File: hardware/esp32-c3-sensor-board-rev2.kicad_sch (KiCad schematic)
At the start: 14 parts, among them J1 BME280_Module, J2 BH1750_Module, J3 Relay, J4 Button, J5 GPIO, U1 ESP32-C3-SuperMini, U2 HLK-LD2410C

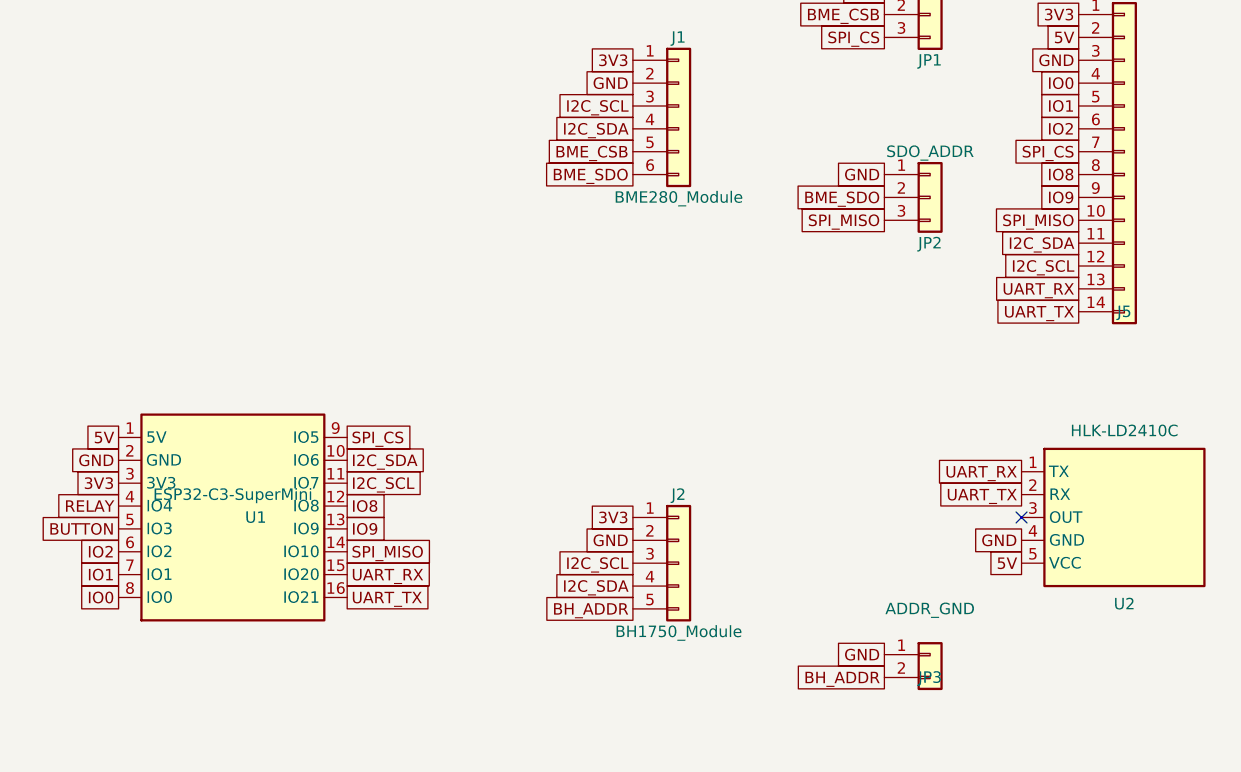
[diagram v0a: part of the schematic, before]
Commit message: Fix ESP32-C3 Super Mini pinout and re-route rev2
- Correct the U1 socket footprint pad order to match the physical module
  (pad 1 = 5V at the USB end, pad 8 = GPIO0, pad 9 = GPIO5, pad 16 = GPIO21).
- Use the reference pinout for I2C: SDA = GPIO8, SCL = GPIO9; free GPIO6/7
  go to the J5 breakout row. UART stays GPIO20/21, relay GPIO4, button GPIO3.
- Add full pin descriptions to the ESP32 symbol and board silkscreen
  (GPIOx plus MISO/MOSI/SS/SDA/SCL/RX/TX), and update all docs.
- Re-route the board against the corrected pin order (FreeRouting);
  DRC 0 errors / 0 unconnected, 2 pre-existing cosmetic silk warnings.
- Regenerate gerbers, drill, job file and the gerber zip.

doorbell.yml still lists GPIO6/7 for I2C and must be updated to
sda: GPIO8 / scl: GPIO9 on the software side.

Co-Authored-By: Claude Code <noreply@anthropic.com>
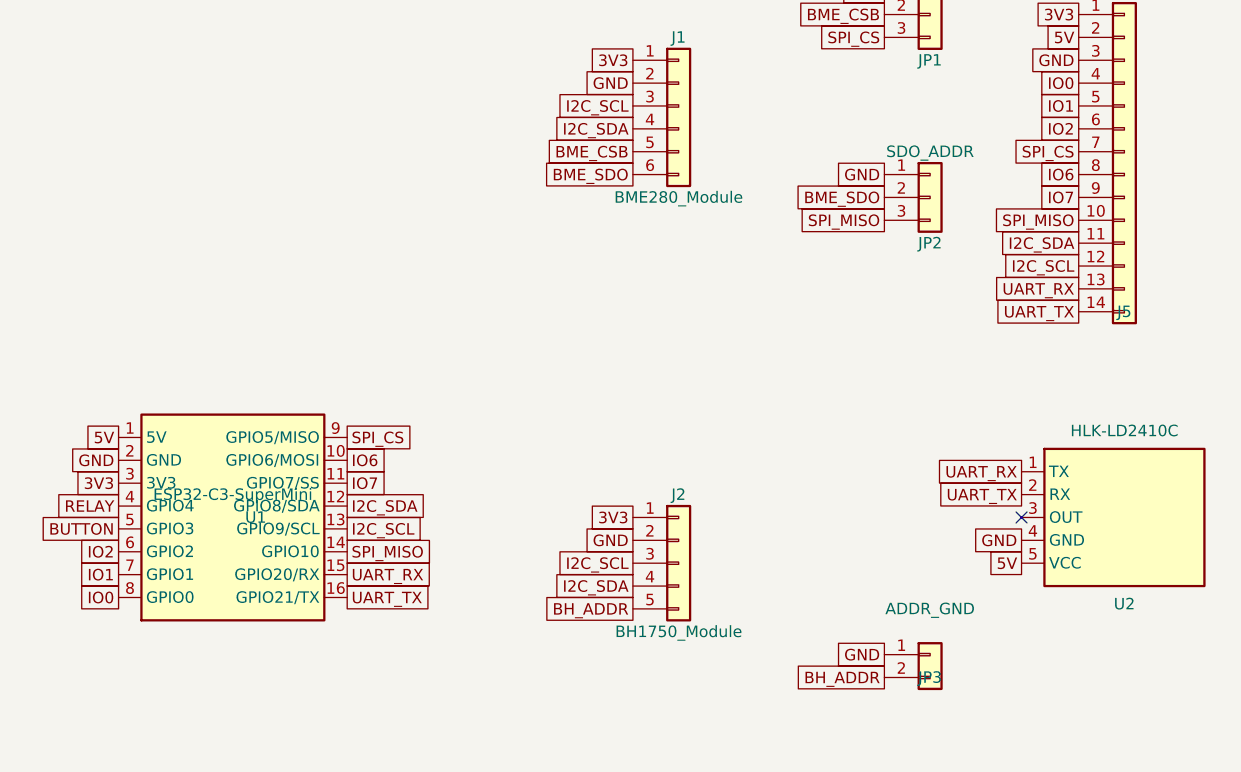
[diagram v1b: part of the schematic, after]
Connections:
- net I2C_SCL: now also U1.13 (GPIO9/SCL); no longer U1.11 (IO7)
- net I2C_SDA: now also U1.12 (GPIO8/SDA); no longer U1.10 (IO6)
- net IO8 renamed IO6
- net IO6: now also U1.10 (GPIO6/MOSI); no longer U1.12 (IO8)
- net IO9 renamed IO7
- net IO7: now also U1.11 (GPIO7/SS); no longer U1.13 (IO9)
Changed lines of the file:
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@@
-		)
-	)
-	(global_label "I2C_SDA"
-		(at 113.03 93.98 0)
-		(effects
-			(font
-				(size 1.27 1.27)
-			)
-			(justify left)
-		)
-	)
-	(global_label "I2C_SCL"
-		(at 113.03 96.52 0)
-		(effects
-			(font
-				(size 1.27 1.27)
-			)
-			(justify left)
 		)
 	)
@@
 		)
 	)
-	(global_label "IO8"
-		(at 113.03 99.06 0)
-		(effects
-			(font
-				(size 1.27 1.27)
-			)
-			(justify left)
-		)
-	)
-	(global_label "IO9"
-		(at 113.03 101.6 0)
-		(effects
-			(font
-				(size 1.27 1.27)
-			)
-			(justify left)
-		)
-	)
 	(symbol
 		(lib_id "Connector_Generic:Conn_01x14")
@@
 		)
 	)
-	(global_label "IO8"
-		(at 194.30999999999997 62.23 180)
-		(effects
-			(font
-				(size 1.27 1.27)
-			)
-			(justify right)
-		)
-	)
-	(global_label "IO9"
-		(at 194.30999999999997 64.77 180)
-		(effects
-			(font
-				(size 1.27 1.27)
-			)
-			(justify right)
-		)
-	)
 	(global_label "SPI_MISO"
 		(at 194.30999999999997 67.31 180)
@@
 		(effects
 			(font
+				(size 1.27 1.27)
+			)
+			(justify right)
+		)
+	)
+	(global_label "IO6"
+		(at 113.03 93.98 0)
+		(effects
+			(font
+				(size 1.27 1.27)
+			)
+			(justify left)
+		)
+	)
+	(global_label "IO7"
+		(at 113.03 96.52 0)
+		(effects
+			(font
+				(size 1.27 1.27)
+			)
+			(justify left)
+		)
+	)
+	(global_label "I2C_SDA"
+		(at 113.03 99.06 0)
+		(effects
+			(font
+				(size 1.27 1.27)
+			)
+			(justify left)
+		)
+	)
+	(global_label "I2C_SCL"
+		(at 113.03 101.6 0)
+		(effects
+			(font
+				(size 1.27 1.27)
+			)
+			(justify left)
+		)
+	)
+	(global_label "IO6"
+		(at 194.31 62.23 180)
+		(effects
+			(font
+				(size 1.27 1.27)
+			)
+			(justify right)
+		)
+	)
+	(global_label "IO7"
+		(at 194.31 64.77 180)
+		(effects
+			(font

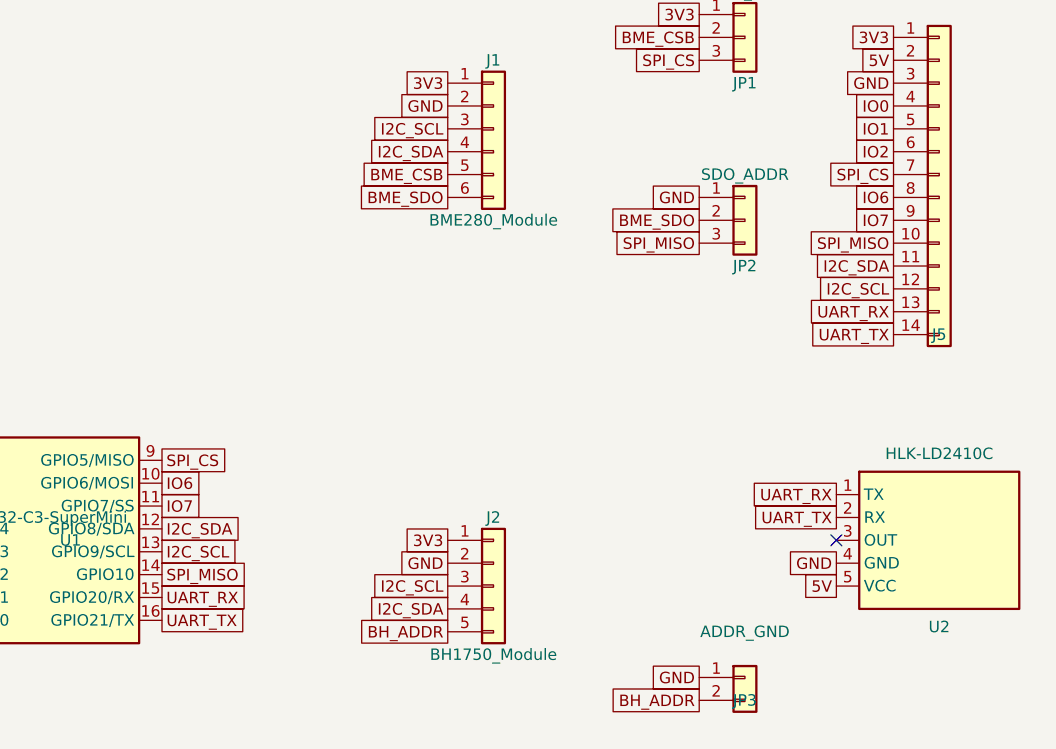
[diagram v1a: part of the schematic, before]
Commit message: Align BME280 SPI option with the ESP32-C3 reference pinout
- SPI_MISO moves from GPIO10 to GPIO5 (reference MISO)
- SPI_CS moves from GPIO5 to GPIO7 (reference SS)
- GPIO10 is now a free J5 breakout pin
- I2C stays SDA=GPIO8 / SCL=GPIO9; UART GPIO20/21; relay GPIO4; button GPIO3
- Re-route the affected nets; DRC 0 errors / 0 unconnected (2 cosmetic silk warnings)
- Update JP1/JP2 silkscreen legends and all pin-map docs
- Regenerate gerbers, drill, job file and gerber zip

The schematic symbol now maps: GPIO5/MISO->SPI_MISO, GPIO7/SS->SPI_CS,
GPIO8/SDA->I2C_SDA, GPIO9/SCL->I2C_SCL, GPIO20/RX->UART_RX, GPIO21/TX->UART_TX.
BME280 SPI mode reuses SCL/SDA as SCK/MOSI (GPIO9/GPIO8), since the module
shares those pins between I2C and SPI.

Co-Authored-By: Claude Code <noreply@anthropic.com>
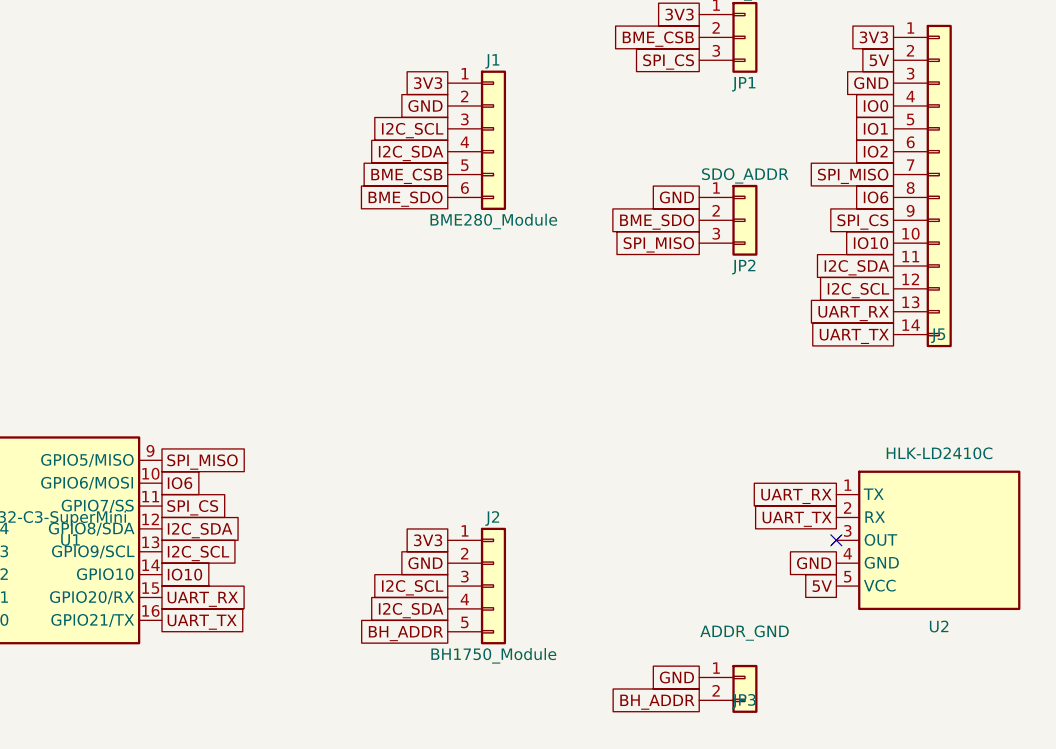
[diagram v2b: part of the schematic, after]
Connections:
- net IO7 is gone; now on net SPI_CS: J5.9 (Pin_9), U1.11 (GPIO7/SS)
- net SPI_CS: no longer J5.7 (Pin_7), U1.9 (GPIO5/MISO)
- net SPI_MISO: now also J5.7 (Pin_7), U1.9 (GPIO5/MISO); no longer J5.10 (Pin_10), U1.14 (GPIO10)
- new net IO10: J5.10 (Pin_10), U1.14 (GPIO10)
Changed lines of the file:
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@@
-		)
-	)
-	(global_label "SPI_CS"
-		(at 113.03 91.44 0)
-		(effects
-			(font
-				(size 1.27 1.27)
-			)
-			(justify left)
-		)
-	)
-	(global_label "SPI_MISO"
-		(at 113.03 104.14 0)
-		(effects
-			(font
-				(size 1.27 1.27)
-			)
-			(justify left)
 		)
 	)
@@
 		)
 	)
-	(global_label "SPI_CS"
-		(at 194.30999999999997 59.69 180)
-		(effects
-			(font
-				(size 1.27 1.27)
-			)
-			(justify right)
-		)
-	)
-	(global_label "SPI_MISO"
-		(at 194.30999999999997 67.31 180)
-		(effects
-			(font
-				(size 1.27 1.27)
-			)
-			(justify right)
-		)
-	)
 	(global_label "I2C_SDA"
 		(at 194.30999999999997 69.85 180)
@@
 		)
 	)
-	(global_label "IO7"
-		(at 113.03 96.52 0)
-		(effects
-			(font
-				(size 1.27 1.27)
-			)
-			(justify left)
-		)
-	)
 	(global_label "I2C_SDA"
 		(at 113.03 99.06 0)
@@
 		)
 	)
-	(global_label "IO7"
+	(global_label "SPI_MISO"
+		(at 113.03 91.44 0)
+		(effects
+			(font
+				(size 1.27 1.27)
+			)
+			(justify left)
+		)
+	)
+	(global_label "SPI_CS"
+		(at 113.03 96.52 0)
+		(effects
+			(font
+				(size 1.27 1.27)
+			)
+			(justify left)
+		)
+	)
+	(global_label "IO10"
+		(at 113.03 104.14 0)
+		(effects
+			(font
+				(size 1.27 1.27)
+			)
+			(justify left)
+		)
+	)
+	(global_label "SPI_MISO"
+		(at 194.31 59.69 180)
+		(effects
+			(font
+				(size 1.27 1.27)
+			)
+			(justify right)
+		)
+	)
+	(global_label "SPI_CS"
 		(at 194.31 64.77 180)
 		(effects
 			(font
+				(size 1.27 1.27)
+			)
+			(justify right)
+		)
+	)
+	(global_label "IO10"
+		(at 194.31 67.31 180)
+		(effects
+			(font

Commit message: Fit J5 as a standard 1x14 female socket
Replace the bare breakout_1x14 footprint with the standard
Connector_PinSocket_2.54mm:PinSocket_1x14_P2.54mm_Vertical at the same
position (40, 25). Pad positions, drills and nets are unchanged; pad 1 is
now the standard rectangular pin-1 marker and the socket has a 3D model.

- Update the schematic J5 Footprint field so a future F8 keeps the socket.
- Update the JLC BOM footprint row and all docs/QUOTE wording (J5 is now a
  fitted socket, not bare holes).
- Refill zones and re-run DRC: 0 errors / 0 unconnected (2 cosmetic silk
  warnings).
- Regenerate gerbers, drill, job file and gerber zip from the final board.

Co-Authored-By: Claude Code <noreply@anthropic.com>
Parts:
- J5: footprint sensor-board:breakout_1x14 -> Connector_PinSocket_2.54mm:PinSocket_1x14_P2.54mm_Vertical
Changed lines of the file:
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@@
 			)
 		)
-		(property "Footprint" "sensor-board:breakout_1x14"
+		(property "Footprint" "Connector_PinSocket_2.54mm:PinSocket_1x14_P2.54mm_Vertical"
 			(at 199.39 59.69 0)
 			(hide yes)
